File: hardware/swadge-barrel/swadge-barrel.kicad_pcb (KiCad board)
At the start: 2 copper layers, 70.4 x 89.6 mm, 48 parts, among them J1 USB_B_Micro, SW1 SW_SPDT, U1 AP1117-33, U2 ESP-13-WROOM-02D, U3 BUS_PCIexpress, U4 OLED_CONNECTOR, U5 QMA6981, U6 OLED_DISPLAY

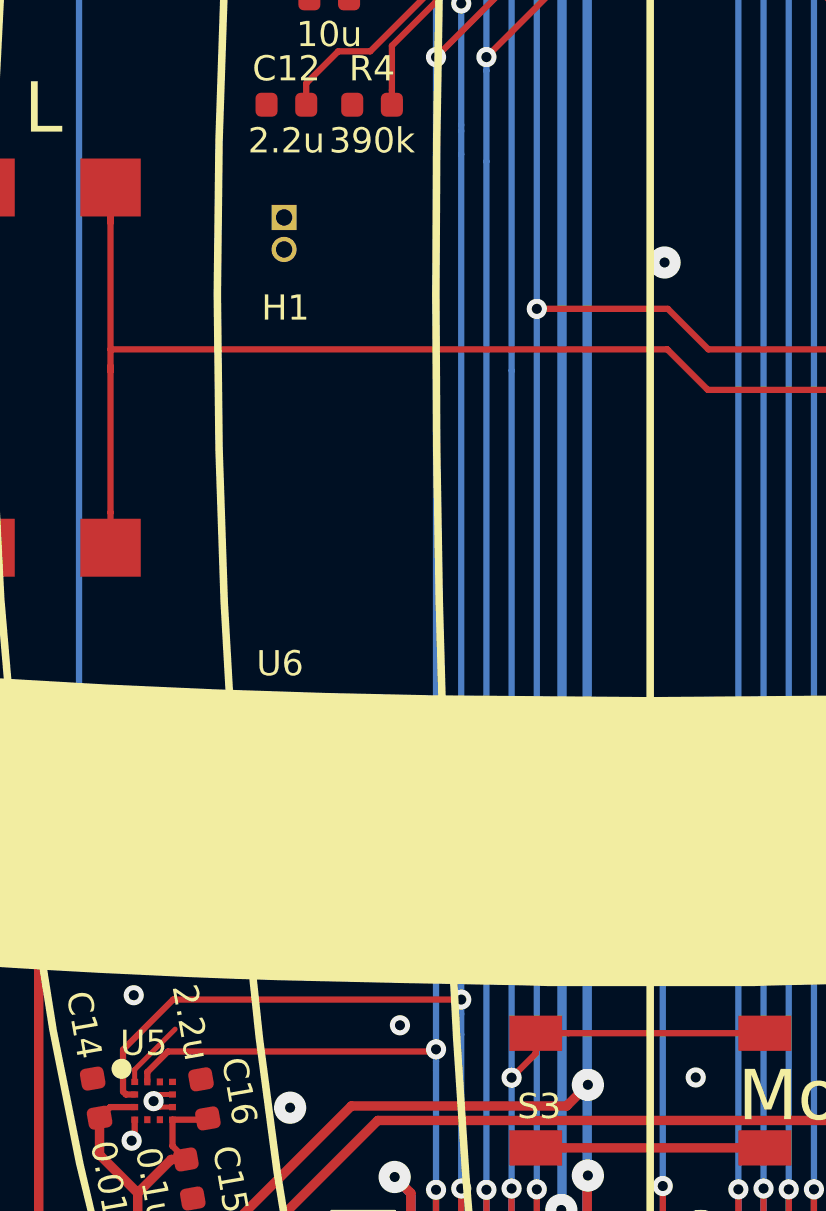
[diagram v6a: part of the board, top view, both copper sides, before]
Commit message: Made I2C traces to accel less right angly
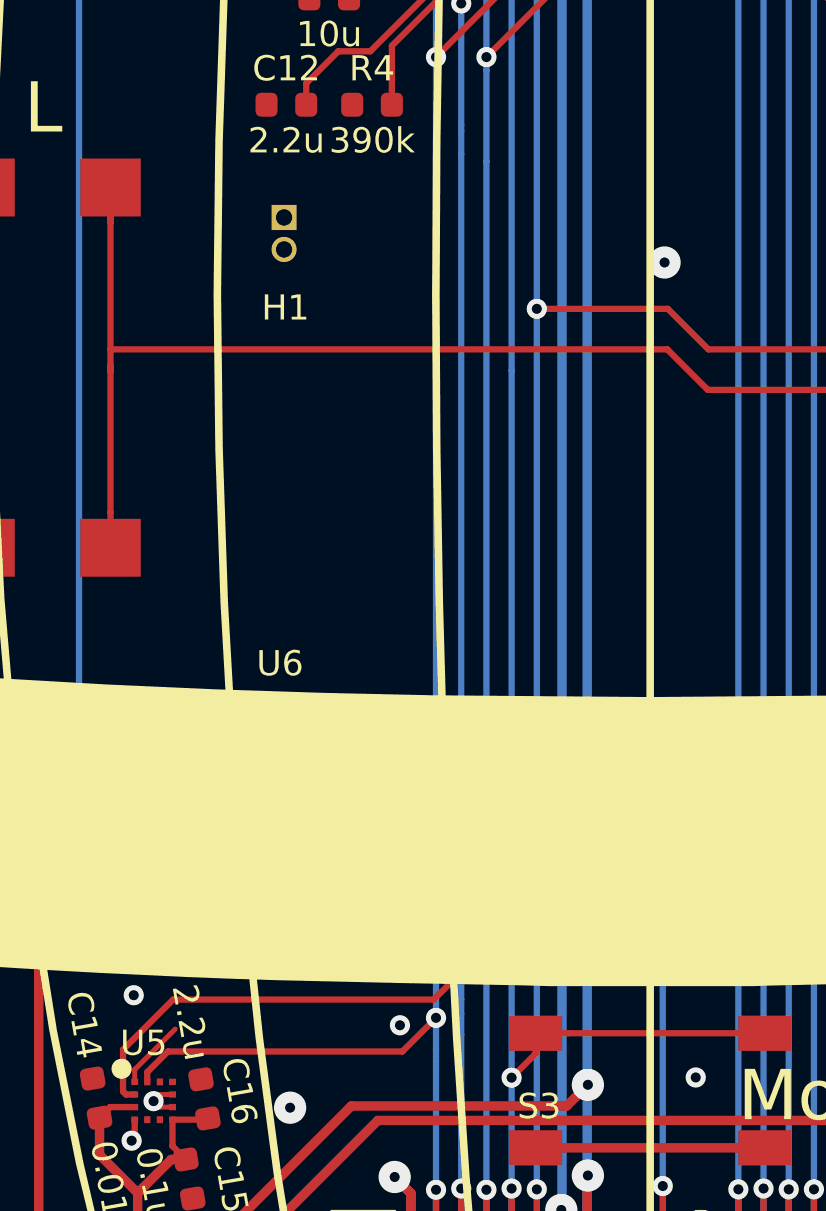
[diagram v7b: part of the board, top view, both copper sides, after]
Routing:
- net SCL: track 133.5 -> 134.0 mm
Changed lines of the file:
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@@
     (thickness 1.6)
     (drawings 398)
-    (tracks 481)
+    (tracks 485)
     (zones 0)
     (modules 48)
@@
   (segment (start 169.149833 120.27778) (end 167.771796 121.655817) (width 0.375) (layer F.Cu) (net 4))
   (segment (start 170.002697 120.27778) (end 169.149833 120.27778) (width 0.375) (layer F.Cu) (net 4))
-  (via (at 143.0191 124.65) (size 1.28) (drill 0.4) (layers F.Cu B.Cu) (net 4))
-  (segment (start 146.2843 123.5) (end 145.1343 124.65) (width 0.375) (layer F.Cu) (net 4))
-  (segment (start 145.1343 124.65) (end 143.0191 124.65) (width 0.375) (layer F.Cu) (net 4))
-  (segment (start 129.817385 124.65) (end 125.872228 120.704843) (width 0.375) (layer F.Cu) (net 4))
-  (segment (start 143.0191 124.65) (end 129.817385 124.65) (width 0.375) (layer F.Cu) (net 4))
   (via (at 148.2 76.45) (size 1.28) (drill 0.4) (layers F.Cu B.Cu) (net 4))
   (segment (start 148.349999 76.300001) (end 148.2 76.45) (width 0.375) (layer F.Cu) (net 4))
@@
   (segment (start 123.9 74.875) (end 123.8875 74.8625) (width 0.375) (layer F.Cu) (net 4))
   (segment (start 143.0468 74.875) (end 123.9 74.875) (width 0.375) (layer F.Cu) (net 4))
+  (via (at 143.0191 124.17274) (size 1.28) (drill 0.4) (layers F.Cu B.Cu) (net 4))
+  (segment (start 142.9937 124.14734) (end 143.0191 124.17274) (width 0.375) (layer F.Cu) (net 4))
+  (segment (start 125.872228 120.704843) (end 129.314725 124.14734) (width 0.375) (layer F.Cu) (net 4))
+  (segment (start 129.314725 124.14734) (end 142.9937 124.14734) (width 0.375) (layer F.Cu) (net 4))
+  (segment (start 143.659099 124.812739) (end 143.0191 124.17274) (width 0.375) (layer F.Cu) (net 4))
+  (segment (start 144.971561 124.812739) (end 143.659099 124.812739) (width 0.375) (layer F.Cu) (net 4))
+  (segment (start 146.2843 123.5) (end 144.971561 124.812739) (width 0.375) (layer F.Cu) (net 4))
   (segment (start 157.036446 86.931965) (end 157.498058 86.470353) (width 0.25) (layer F.Cu) (net 5))
   (segment (start 156.698048 87.270363) (end 157.036446 86.931965) (width 0.25) (layer F.Cu) (net 5))
@@
   (segment (start 167.931036 65.329088) (end 167.931036 63.810624) (width 0.25) (layer F.Cu) (net 15))
   (segment (start 136.9916 129.0084) (end 136.9916 128.6684) (width 0.25) (layer B.Cu) (net 15))
-  (segment (start 136.906 128.27) (end 136.9916 128.1844) (width 0.25) (layer F.Cu) (net 15))
   (segment (start 136.9916 128.6684) (end 136.9916 128.1844) (width 0.25) (layer B.Cu) (net 15))
   (segment (start 136.9916 128.1844) (end 136.9916 93.6416) (width 0.25) (layer B.Cu) (net 15))
   (segment (start 125.5308 129.4758) (end 125.5308 129.0883) (width 0.25) (layer F.Cu) (net 15))
   (segment (start 125.5308 129.0883) (end 126.3491 128.27) (width 0.25) (layer F.Cu) (net 15))
-  (segment (start 126.3491 128.27) (end 136.906 128.27) (width 0.25) (layer F.Cu) (net 15))
-  (via (at 136.9916 128.1844) (size 0.8) (drill 0.4) (layers F.Cu B.Cu) (net 15))
+  (via (at 136.9916 126.9334) (size 0.8) (drill 0.4) (layers F.Cu B.Cu) (net 15))
+  (segment (start 126.3491 128.27) (end 135.655 128.27) (width 0.25) (layer F.Cu) (net 15))
+  (segment (start 135.655 128.27) (end 136.9916 126.9334) (width 0.25) (layer F.Cu) (net 15))
   (via (at 137.9916 133.7084) (size 0.8) (drill 0.4) (layers F.Cu B.Cu) (net 16))
   (segment (start 137.9916 139.7174) (end 137.9916 133.7084) (width 0.25) (layer F.Cu) (net 16))
@@
   (segment (start 150.175 69.5) (end 149.9 69.5) (width 0.25) (layer F.Cu) (net 16))
   (segment (start 156.85 62.825) (end 150.175 69.5) (width 0.25) (layer F.Cu) (net 16))
-  (segment (start 137.9916 126.2084) (end 137.9916 92.6584) (width 0.25) (layer B.Cu) (net 16))
   (segment (start 137.9916 92.6584) (end 137.9916 91.7334) (width 0.25) (layer B.Cu) (net 16))
   (segment (start 137.9916 91.7334) (end 137.9916 91.4916) (width 0.25) (layer B.Cu) (net 16))
@@
   (segment (start 137.9916 126.7784) (end 137.9916 126.2084) (width 0.25) (layer B.Cu) (net 16))
   (segment (start 137.9916 127.5916) (end 137.9916 126.7784) (width 0.25) (layer B.Cu) (net 16))
-  (segment (start 126.55519 126.2084) (end 137.9916 126.2084) (width 0.25) (layer F.Cu) (net 16))
   (segment (start 124.568299 128.195291) (end 126.55519 126.2084) (width 0.25) (layer F.Cu) (net 16))
   (segment (start 124.568299 129.860801) (end 124.568299 128.195291) (width 0.25) (layer F.Cu) (net 16))
   (segment (start 124.683298 129.9758) (end 124.568299 129.860801) (width 0.25) (layer F.Cu) (net 16))
   (segment (start 125.0308 129.9758) (end 124.683298 129.9758) (width 0.25) (layer F.Cu) (net 16))
-  (via (at 137.9916 126.2084) (size 0.8) (drill 0.4) (layers F.Cu B.Cu) (net 16))
+  (via (at 137.9916 125.11888) (size 0.8) (drill 0.4) (layers F.Cu B.Cu) (net 16))
+  (segment (start 136.90208 126.2084) (end 137.9916 125.11888) (width 0.25) (layer F.Cu) (net 16))
+  (segment (start 126.55519 126.2084) (end 136.90208 126.2084) (width 0.25) (layer F.Cu) (net 16))
+  (segment (start 137.9916 126.2084) (end 137.9916 125.11888) (width 0.25) (layer B.Cu) (net 16))
+  (segment (start 137.9916 125.11888) (end 137.9916 92.6584) (width 0.25) (layer B.Cu) (net 16))
   (via (at 138.9916 133.7584) (size 0.8) (drill 0.4) (layers F.Cu B.Cu) (net 17))
   (segment (start 138.9916 139.7174) (end 138.9916 133.7584) (width 0.25) (layer F.Cu) (net 17))

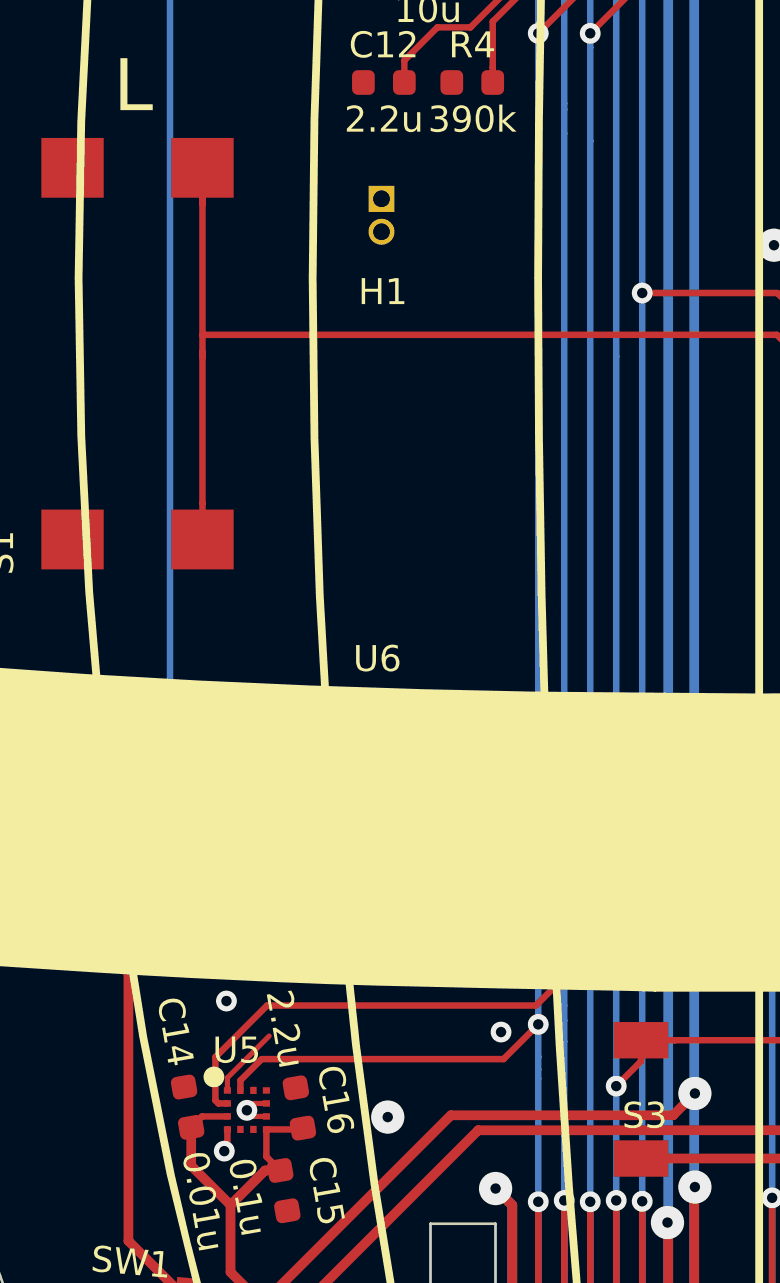
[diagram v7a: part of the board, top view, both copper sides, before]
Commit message: Added series I2C resistors to QMA6981
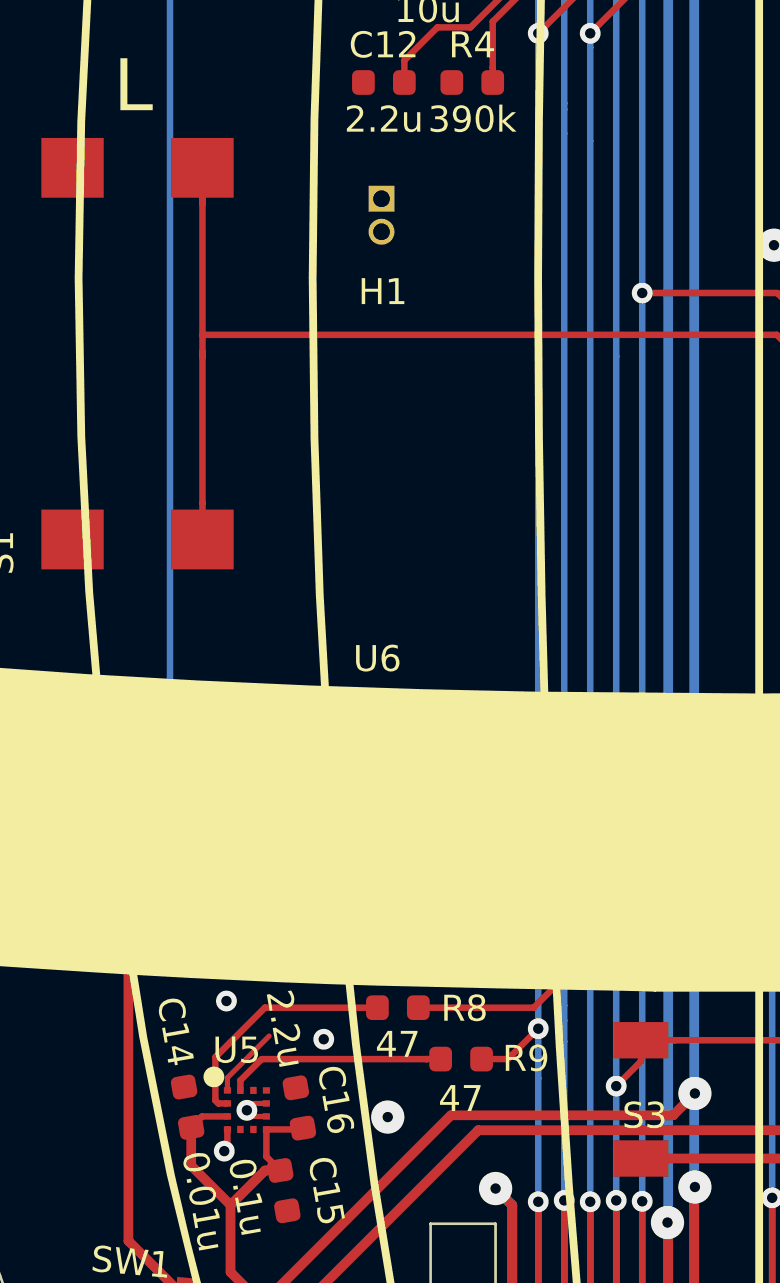
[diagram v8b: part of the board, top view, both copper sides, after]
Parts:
- added R8: 47, Swadge_Parts:R_0603_1608Metric, F.Cu at (131.6, 126.3)
- added R9: 47, Swadge_Parts:R_0603_1608Metric, F.Cu at (134.0, 128.3)
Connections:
- U5 pad 12: SCL -> Net-(R9-Pad2)
- U5 pad 2: SDA -> Net-(R8-Pad1)
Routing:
- net SDA: track 133.5 -> 122.8 mm
- net SCL: track 134.0 -> 123.9 mm
- net Net-(R8-Pad1): track 0.00 -> 9.20 mm
- net Net-(R9-Pad2): track 0.00 -> 8.43 mm
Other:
- board text added: "Barrel 1.0.5"
- board text removed: "Barrel 1.0.4"
